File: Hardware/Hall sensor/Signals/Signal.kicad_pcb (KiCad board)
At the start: 2 copper layers, 72.6 x 35.6 mm, 47 parts, among them Q1 Q_NPN_Darlington_BEC, U1 Signals_MCC, U2 LM324, U3 LM324, U4 LM324

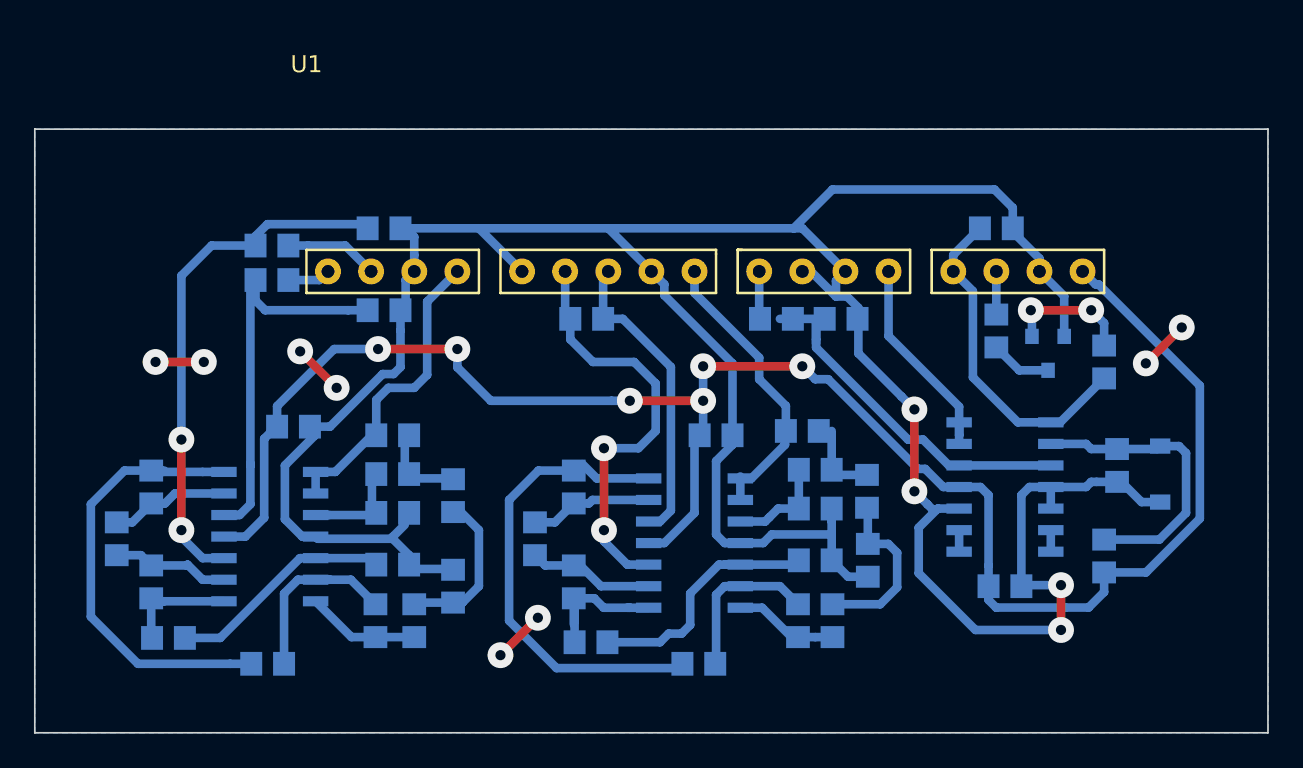
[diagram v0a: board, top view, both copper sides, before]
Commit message: Signals revisado. Foram reduzidos os jjumpers, GERBERS gerados e .wrl exportado.
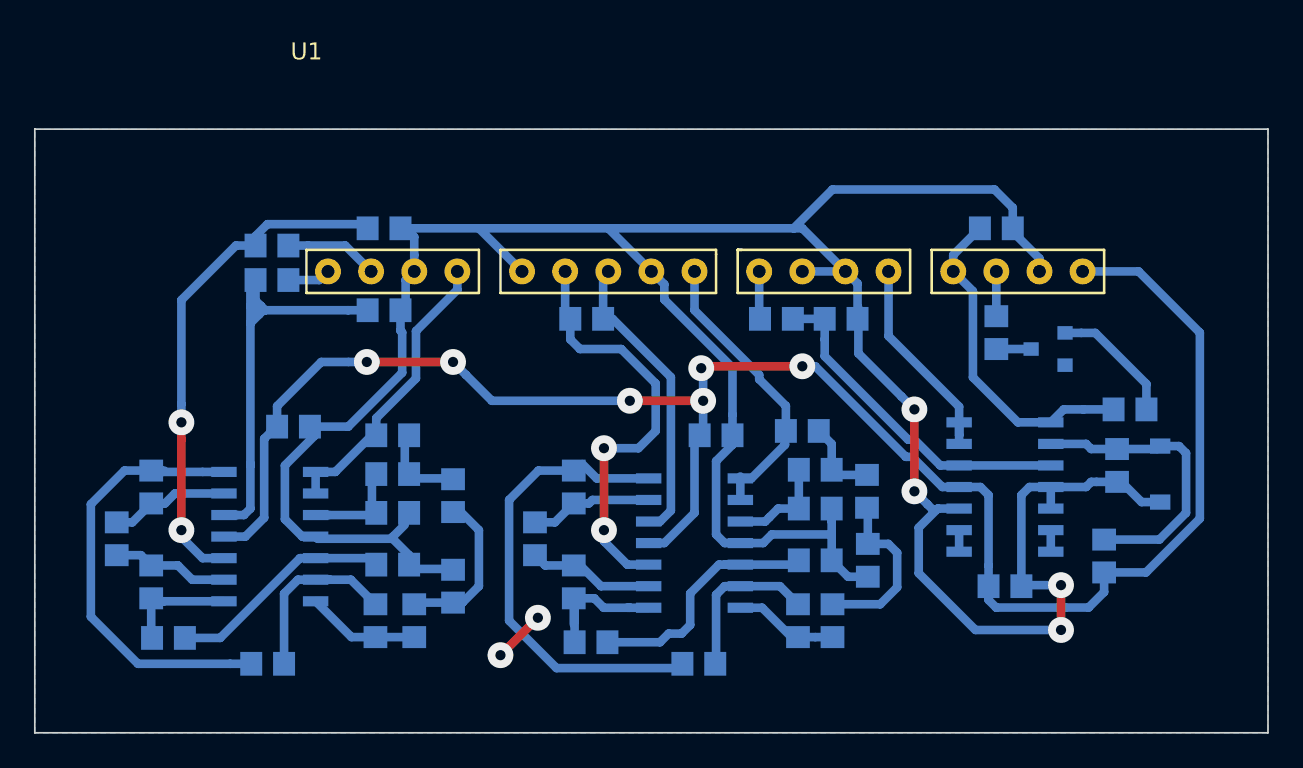
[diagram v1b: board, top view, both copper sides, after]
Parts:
- moved R3 3.18 mm to (77.0, 28.4), turned to 0 degrees
- moved Q1 0.25 mm to (72.1, 24.9), turned to 180 degrees
- moved R4 0.10 mm to (69.1, 23.9)
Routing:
- net GNDA: track 192.3 -> 179.1 mm, vias 12 -> 6
- net Net-(R32-Pad1): track 24.1 -> 26.6 mm
- net /Vbat_SIG: track 22.0 -> 20.1 mm
- net Net-(Q1-Pad3): track 3.61 -> 2.05 mm
- net Vpanel: track 18.9 -> 18.0 mm
- net Net-(R30-Pad1): track 31.1 -> 30.2 mm
- net +5VA: track 109.2 -> 109.8 mm
- net Net-(Q1-Pad1): track 7.52 -> 7.54 mm, vias 2 -> 0

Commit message: Fixed voltage divider The old voltage divider isn't differential
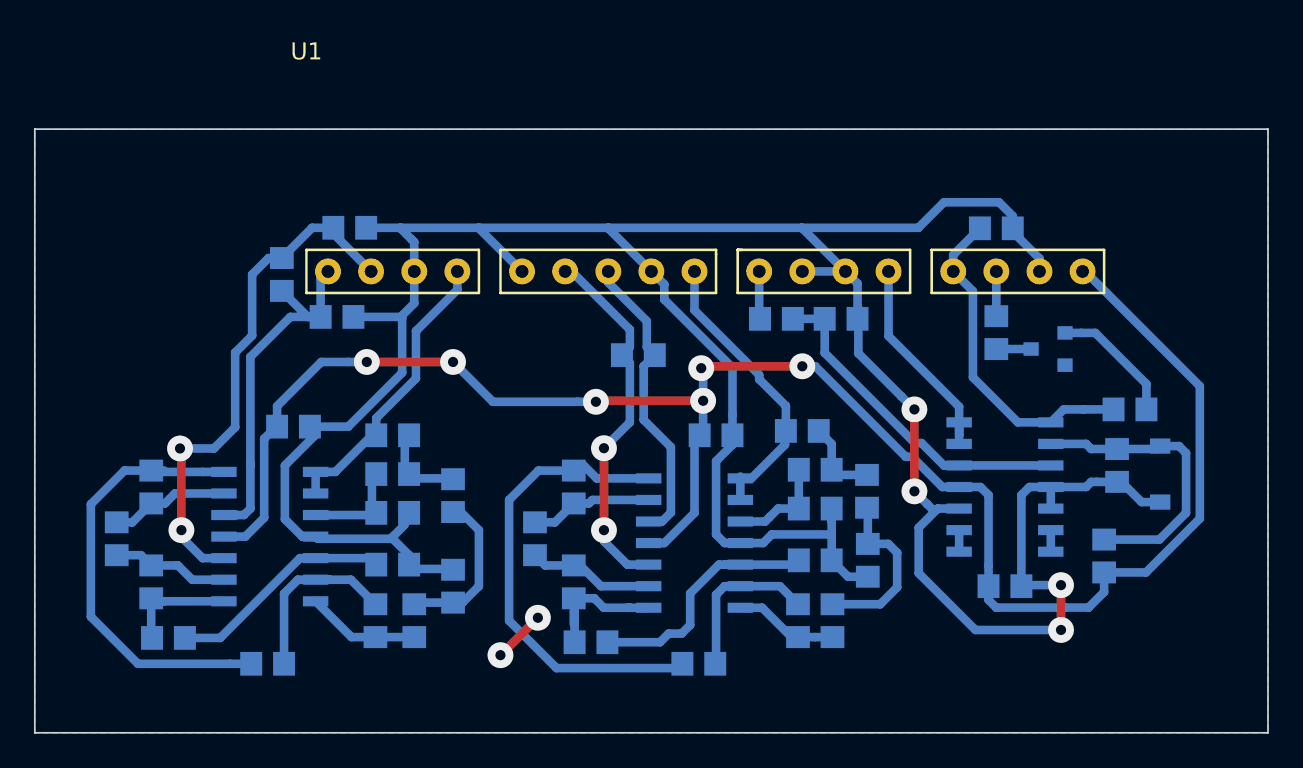
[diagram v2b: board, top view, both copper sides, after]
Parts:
- removed R30: ??, Resistor_SMD:R_0805_2012Metric_Pad1.29x1.40mm_HandSolder
- moved R_shunt1 3.72 mm to (48.0, 25.2)
- moved R32 2.80 mm to (30.2, 23.0)
- moved R31 2.02 mm to (31.0, 17.8)
- moved R35 0.67 mm to (27.0, 20.5), turned to 270 degrees
- turned R34 to 180 degrees
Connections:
- net BatOVInterrupt renamed /BatOVInterrupt
- net Ipanel renamed /Ipanel
- net Ipanel_Ref renamed /Ipanel_Ref
- net Ipanel_SIG renamed /Ipanel_SIG
- net PWM renamed /PWM
- net Vbat renamed /Vbat
- net Vpanel renamed /Vpanel
- R31 pad 2: Net-(R30-Pad1) -> /Vpanel_SIG
- R32 pad 1: Net-(R32-Pad1) -> /Vpanel_Ref
- R33 pad 1: /Vbat_SIG -> Net-(R33-Pad1)
- R34 pad 1: Vbat_SIG_IN -> Net-(R33-Pad1)
- R34 pad 2: /Vbat_SIG -> /Vbat_SIG_IN
- R35 pad 1: Net-(R32-Pad1) -> /Vpanel_SIG
- R35 pad 2: Vpanel_Ref -> /Vpanel_Ref
- U1 pad 1: Vpanel_Ref -> /Vpanel_Ref
- U1 pad 10: Vbat_SIG_IN -> /Vbat_SIG_IN
- U1 pad 2: Vpanel_SIG -> /Vpanel_SIG
- U2 pad 10: /Vbat_SIG -> Net-(R33-Pad1)
- U2 pad 5: /Vbat_SIG -> Net-(R33-Pad1)
- U4 pad 3: Net-(R30-Pad1) -> /Vpanel_SIG
- U4 pad 4: +5VA -> Net-(U4-Pad4)
- U4 pad 5: Net-(R32-Pad1) -> /Vpanel_Ref
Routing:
- net /Vpanel_SIG: track 0.00 -> 30.4 mm, vias 0 -> 2
- net Net-(R30-Pad1): track 30.2 -> 0.00 mm, vias 2 -> 0
- net Net-(R32-Pad1): track 26.6 -> 0.00 mm
- net /Vpanel_Ref: track 0.00 -> 22.4 mm
- net /Vbat_SIG: track 20.1 -> 0.00 mm
- net Net-(R33-Pad1): track 0.00 -> 19.9 mm
- net Vpanel_SIG: track 5.51 -> 0.00 mm
- net GNDA: track 179.1 -> 182.4 mm
- net /Ipanel_SIG: track 25.1 -> 22.0 mm
- net Vbat_SIG_IN: track 2.61 -> 0.00 mm
- net /Vbat_SIG_IN: track 0.00 -> 2.61 mm
- net Vpanel_Ref: track 2.54 -> 0.00 mm
- net +5VA: track 109.8 -> 108.0 mm
